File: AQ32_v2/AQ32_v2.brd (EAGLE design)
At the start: 57.1 x 57.1 mm, 117 parts, among them Q2 BCV27, Q3 BCV27, Q5 BCV27, Q6 BCV27, U1 ITG-3200, U10 MS5611, U11 MIC5239, U13 74AHC1G86DCK, U2 STM32F10XVXT6, U3 74AHC1G86DCK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

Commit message: Changes from ala42 20130428
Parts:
- moved R48 0.32 mm to (43.1, 20.3)
- moved R49 0.32 mm to (43.1, 19.1)
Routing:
- net 3V3DIG: track 233.6 -> 235.5 mm
- net MPU_CS: track 30.3 -> 31.8 mm
- net HMC_INT: track 20.2 -> 19.0 mm
- net MISO3_LV: track 47.0 -> 48.0 mm
- net GND: vias 90 -> 93

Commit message: Isolate BM/LED GND from main GND using 0R resistor. More clearance around holes.
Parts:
- added R39: 0R, SparkFun:C0402
- moved C3 0.84 mm to (5.56, 12.6)
- moved C11 0.83 mm to (2.83, 12.6)
- moved C9 0.83 mm to (8.29, 12.6)
- moved C8 0.32 mm to (11.5, 47.6), turned to 90 degrees
- moved R1 0.25 mm to (9.08, 47.6)
- moved R3 0.25 mm to (10.3, 47.6), turned to 270 degrees
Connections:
- new net GND2: JP1.1, Q2.2, Q3.2, Q5.2, Q6.2, R39.2
- net GND: now also R39.1; no longer JP1.1, Q2.2, Q3.2, Q5.2, Q6.2
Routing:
- net GND2: track 0.00 -> 21.9 mm
- net JTAG-TRST: track 130.3 -> 128.1 mm
- net 5V-3: track 77.7 -> 76.0 mm
- net LIPO: track 7.98 -> 7.21 mm
- net SDA2_LV: track 66.5 -> 65.7 mm
- net UART1_TX: track 88.3 -> 87.7 mm
- net 3V3DIG: track 235.5 -> 234.9 mm
- net GND: track 240.5 -> 239.9 mm, vias 93 -> 89

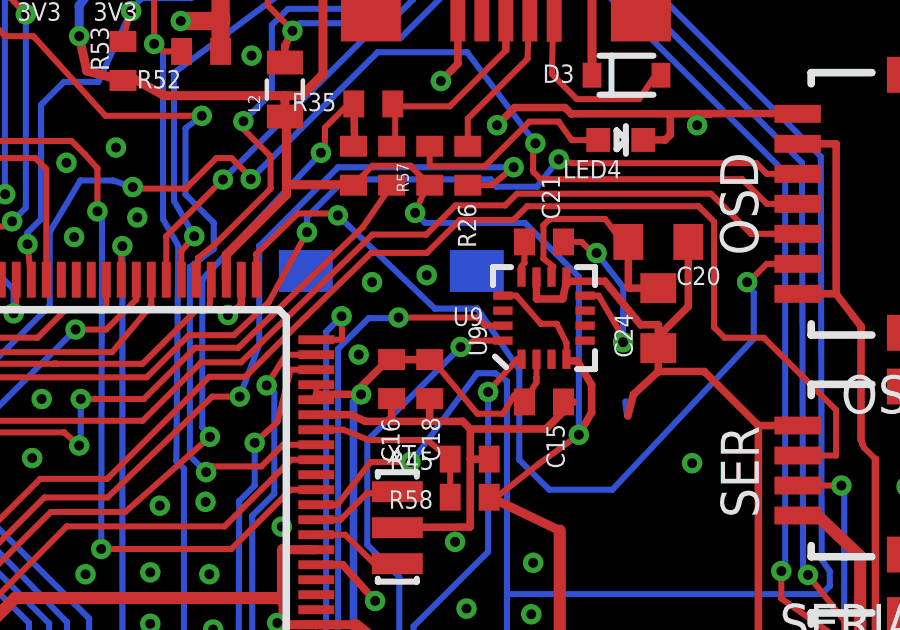
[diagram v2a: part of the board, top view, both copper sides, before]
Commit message: Remove traces under mag.
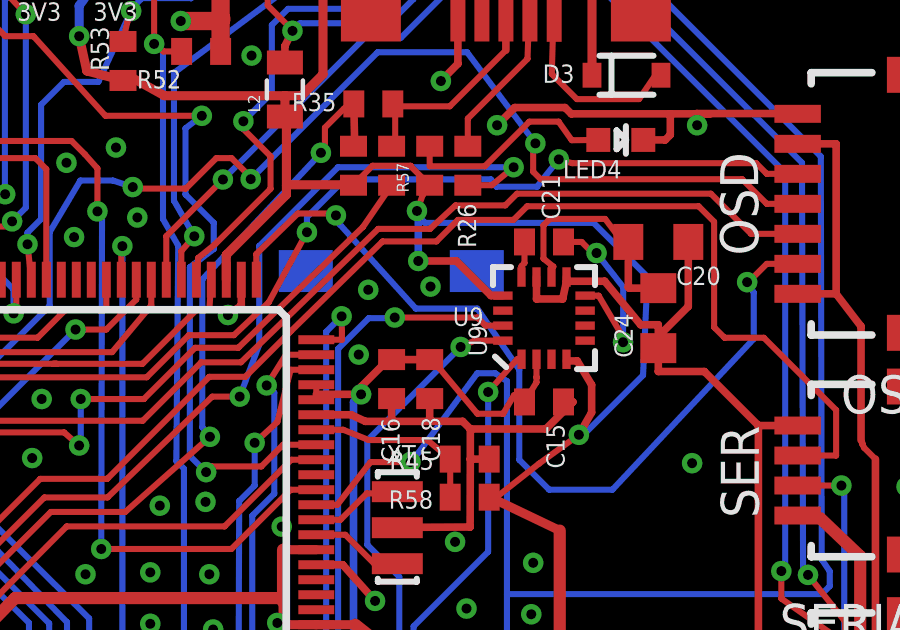
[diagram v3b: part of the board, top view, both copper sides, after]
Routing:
- net 3V3DIG: track 234.9 -> 239.4 mm, vias 9 -> 10
- net GND: track 239.9 -> 237.6 mm

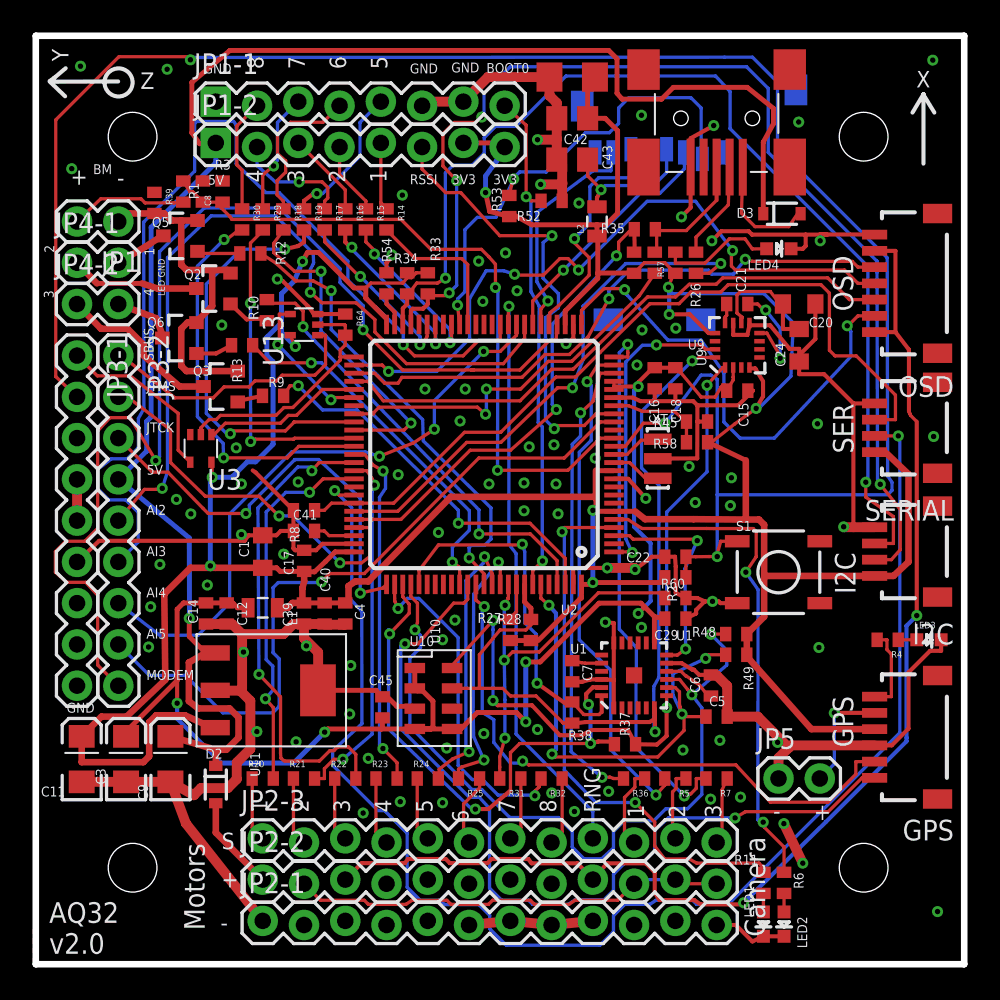
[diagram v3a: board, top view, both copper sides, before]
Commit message: Ala42 added HMC5983 support, remapped receiver/motor lines to match v1 board, moved mag to avoid interference, made space for standoffs by moving uSD conenctor, made power lines thicker
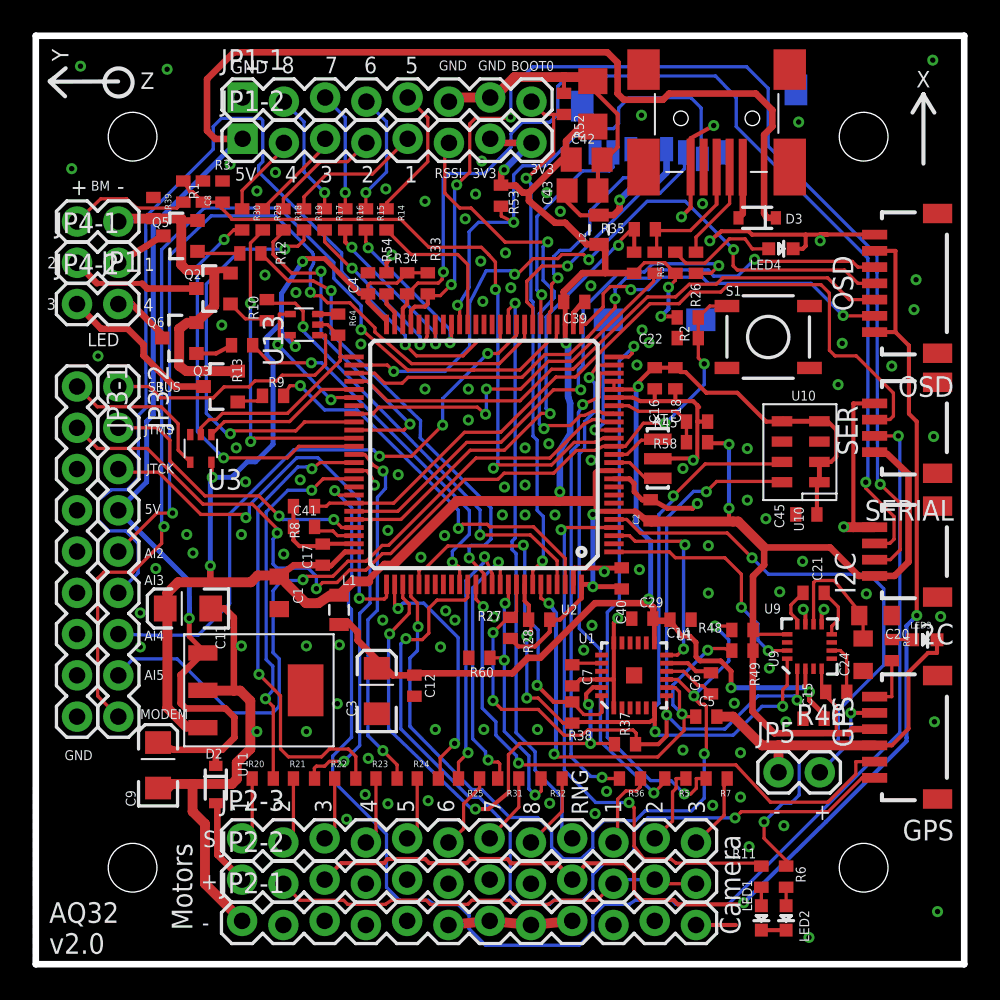
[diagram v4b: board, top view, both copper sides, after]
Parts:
- added C2: 0.1uF, SparkFun:C0402
- added R40: 0R, resistor:R0402
- C42: value 220uF -> 47uF
- C44: value 47uF -> 220uF
- moved C14 29.2 mm to (39.7, 21.2), turned to 0 degrees
- moved C45 28.7 mm to (47.4, 27.7), turned to 180 degrees
- moved U10 27.3 mm to (47.1, 31.6), turned to 180 degrees
- moved C39 25.4 mm to (33.1, 40.8), turned to 0 degrees
- moved C15 20.7 mm to (47.9, 15.1), turned to 180 degrees
- moved C4 20.4 mm to (20.4, 41.9), turned to 90 degrees
- moved C20 19.7 mm to (51.7, 21.5)
- moved C24 19.5 mm to (50.9, 19.1)
- moved U9 19.1 mm to (47.6, 19.6)
- moved C40 18.4 mm to (36.1, 23.7), turned to 90 degrees
- moved C21 18.4 mm to (47.9, 22.9)
- moved R2 16.0 mm to (40.1, 39.8)
- moved C3 16.0 mm to (21.0, 16.8)
- moved S1 14.5 mm to (45.1, 38.6)
- moved C22 13.5 mm to (40.1, 38.5)
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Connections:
- new net N$4: R40.1, U9.6
- net 3V3DIG: now also C2.1, R40.2
- net ADC123_IN11: now also U7.CD1
- net GND: now also C2.2; no longer U7.CD1
- net JTDI/TIM2_CH1: now also R24.2; no longer R32.2
- net JTDO/TIM2_CH2: now also R25.2; no longer R24.2
- net RCV1: now also R19.1; no longer R14.1
- net RCV2: now also R18.1; no longer R15.1
- net RCV3: now also R29.1; no longer R16.1
- net RCV4: now also R30.1; no longer R17.1
- net RCV5: now also R14.1; no longer R19.1
- net RCV6: now also R15.1; no longer R18.1
- net RCV7: now also R16.1; no longer R29.1
- net RCV8: now also R17.1; no longer R30.1
- net TIM3_CH1: now also R31.2; no longer R25.2
- net TIM3_CH2: now also R32.2; no longer R31.2
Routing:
- net GND: track 237.6 -> 161.7 mm, vias 89 -> 120
- net JTAG-TRST: track 128.1 -> 56.4 mm, vias 3 -> 4
- net 3V3DIG: track 239.4 -> 212.9 mm, vias 10 -> 13
- net 3V3AN: track 88.5 -> 78.4 mm, vias 6 -> 4
- net TIM5_CH4: track 30.1 -> 20.9 mm
- net LED2: track 31.2 -> 40.1 mm
- net ADC123_IN11: track 0.00 -> 8.37 mm, vias 0 -> 1
- net TIM3_CH2: track 23.9 -> 16.1 mm
- net NSS1_LV/DAC_OUT1: track 71.2 -> 64.9 mm
- net JTMS: track 23.6 -> 17.8 mm
- net JTDI/TIM2_CH1: track 21.1 -> 15.5 mm
- net SCL1_LV: track 49.6 -> 55.1 mm, vias 4 -> 5
- net RCV1: track 4.20 -> 8.61 mm
- net HMC_INT: track 19.2 -> 15.0 mm
- net VBUS: track 7.23 -> 3.23 mm
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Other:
- board text added: "LED"
- board text removed: "LED GND"
- board text removed: "SOC Robotics"
